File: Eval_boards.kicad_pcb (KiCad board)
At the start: 2 copper layers, 36 parts, among them J1 TC2030, J2 Conn_01x03_Pin, J3 Conn_02x07_Odd_Even, J4 Conn_01x07_Pin, J5 Conn_01x04_Pin, J6 Conn_02x07_Odd_Even, U1 STM32U031K8Ux, Y1 G83270025

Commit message: Early pcb project
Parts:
- removed J5: Conn_01x04_Pin, Connector_PinHeader_2.54mm:PinHeader_1x04_P2.54mm_Vertical
- removed J6: Conn_02x07_Odd_Even, Connector_PinHeader_2.54mm:PinHeader_2x07_P2.54mm_Vertical
- added C10: 40u, Capacitor_SMD:C_0603_1608Metric, B.Cu at (115.0, 85.3)
- added C11: 47n, Capacitor_SMD:C_0603_1608Metric, B.Cu at (116.6, 88.8)
- added C12: 40u, Capacitor_SMD:C_0603_1608Metric, B.Cu at (118.0, 92.7)
- added C13: 10u, Capacitor_SMD:C_0603_1608Metric, B.Cu at (132.2, 90.5)
- added C14: 4u7, Capacitor_SMD:C_0603_1608Metric, B.Cu at (113.5, 85.3)
- added C15: 10u, Capacitor_SMD:C_0603_1608Metric, B.Cu at (114.0, 95.0)
- added C16: 22u, Capacitor_SMD:C_0603_1608Metric, B.Cu at (107.6, 92.0)
- added C8: 1u, Capacitor_SMD:C_0603_1608Metric, B.Cu at (119.5, 82.0)
- added C9: 100n, Capacitor_SMD:C_0603_1608Metric, B.Cu at (118.0, 80.5)
- added D10: blue led, Diode_SMD:D_0603_1608Metric, F.Cu at (115.0, 75.0)
- added D100: blue led, Diode_SMD:D_0603_1608Metric, F.Cu at (95.0, 110.0)
- added D101: blue led, Diode_SMD:D_0603_1608Metric, F.Cu at (100.0, 110.0)
- added D102: blue led, Diode_SMD:D_0603_1608Metric, F.Cu at (105.0, 110.0)
- added D103: blue led, Diode_SMD:D_0603_1608Metric, F.Cu at (110.0, 110.0)
- added D104: blue led, Diode_SMD:D_0603_1608Metric, F.Cu at (115.0, 110.0)
- added D105: blue led, Diode_SMD:D_0603_1608Metric, F.Cu at (120.0, 110.0)
- added D106: blue led, Diode_SMD:D_0603_1608Metric, F.Cu at (125.0, 110.0)
- added D107: blue led, Diode_SMD:D_0603_1608Metric, F.Cu at (130.0, 110.0)
- added D108: blue led, Diode_SMD:D_0603_1608Metric, F.Cu at (135.0, 110.0)
- added D109: blue led, Diode_SMD:D_0603_1608Metric, F.Cu at (140.0, 110.0)
- added D11: blue led, Diode_SMD:D_0603_1608Metric, F.Cu at (120.0, 75.0)
- added D110: blue led, Diode_SMD:D_0603_1608Metric, F.Cu at (145.0, 110.0)
- added D111: blue led, Diode_SMD:D_0603_1608Metric, F.Cu at (150.0, 110.0)
- added D112: blue led, Diode_SMD:D_0603_1608Metric, F.Cu at (155.0, 110.0)
- added D113: blue led, Diode_SMD:D_0603_1608Metric, F.Cu at (85.0, 115.0)
- added D114: blue led, Diode_SMD:D_0603_1608Metric, F.Cu at (90.0, 115.0)
- added D115: blue led, Diode_SMD:D_0603_1608Metric, F.Cu at (95.0, 115.0)
- added D116: blue led, Diode_SMD:D_0603_1608Metric, F.Cu at (100.0, 115.0)
- added D117: blue led, Diode_SMD:D_0603_1608Metric, F.Cu at (105.0, 115.0)
- added D118: blue led, Diode_SMD:D_0603_1608Metric, F.Cu at (110.0, 115.0)
- added D119: blue led, Diode_SMD:D_0603_1608Metric, F.Cu at (115.0, 115.0)
- added D12: blue led, Diode_SMD:D_0603_1608Metric, F.Cu at (125.0, 75.0)
- added D120: blue led, Diode_SMD:D_0603_1608Metric, F.Cu at (120.0, 115.0)
- added D121: blue led, Diode_SMD:D_0603_1608Metric, F.Cu at (125.0, 115.0)
- added D122: blue led, Diode_SMD:D_0603_1608Metric, F.Cu at (130.0, 115.0)
- added D123: blue led, Diode_SMD:D_0603_1608Metric, F.Cu at (135.0, 115.0)
- added D124: blue led, Diode_SMD:D_0603_1608Metric, F.Cu at (140.0, 115.0)
- added D125: blue led, Diode_SMD:D_0603_1608Metric, F.Cu at (145.0, 115.0)
- added D126: blue led, Diode_SMD:D_0603_1608Metric, F.Cu at (150.0, 115.0)
- added D127: blue led, Diode_SMD:D_0603_1608Metric, F.Cu at (155.0, 115.0)
- added D128: blue led, Diode_SMD:D_0603_1608Metric, F.Cu at (90.0, 120.0)
- added D129: blue led, Diode_SMD:D_0603_1608Metric, F.Cu at (95.0, 120.0)
- added D13: blue led, Diode_SMD:D_0603_1608Metric, F.Cu at (130.0, 75.0)
- added D130: blue led, Diode_SMD:D_0603_1608Metric, F.Cu at (100.0, 120.0)
- added D131: blue led, Diode_SMD:D_0603_1608Metric, F.Cu at (105.0, 120.0)
- added D132: blue led, Diode_SMD:D_0603_1608Metric, F.Cu at (110.0, 120.0)
- added D133: blue led, Diode_SMD:D_0603_1608Metric, F.Cu at (115.0, 120.0)
- added D134: blue led, Diode_SMD:D_0603_1608Metric, F.Cu at (120.0, 120.0)
- added D135: blue led, Diode_SMD:D_0603_1608Metric, F.Cu at (125.0, 120.0)
- added D136: blue led, Diode_SMD:D_0603_1608Metric, F.Cu at (130.0, 120.0)
- added D137: blue led, Diode_SMD:D_0603_1608Metric, F.Cu at (135.0, 120.0)
- added D138: blue led, Diode_SMD:D_0603_1608Metric, F.Cu at (140.0, 120.0)
- added D139: blue led, Diode_SMD:D_0603_1608Metric, F.Cu at (145.0, 120.0)
- added D14: blue led, Diode_SMD:D_0603_1608Metric, F.Cu at (135.0, 75.0)
- added D140: blue led, Diode_SMD:D_0603_1608Metric, F.Cu at (150.0, 120.0)
- added D141: blue led, Diode_SMD:D_0603_1608Metric, F.Cu at (89.8, 125.0)
- added D142: blue led, Diode_SMD:D_0603_1608Metric, F.Cu at (95.0, 125.0)
- added D143: blue led, Diode_SMD:D_0603_1608Metric, F.Cu at (100.0, 125.0)
- added D144: blue led, Diode_SMD:D_0603_1608Metric, F.Cu at (105.0, 125.0)
- added D145: blue led, Diode_SMD:D_0603_1608Metric, F.Cu at (110.0, 125.0)
- added D146: blue led, Diode_SMD:D_0603_1608Metric, F.Cu at (115.0, 125.0)
- added D147: blue led, Diode_SMD:D_0603_1608Metric, F.Cu at (120.0, 125.0)
- added D148: blue led, Diode_SMD:D_0603_1608Metric, F.Cu at (125.0, 125.0)
- added D149: blue led, Diode_SMD:D_0603_1608Metric, F.Cu at (130.0, 125.0)
- added D15: blue led, Diode_SMD:D_0603_1608Metric, F.Cu at (140.0, 75.0)
- added D150: blue led, Diode_SMD:D_0603_1608Metric, F.Cu at (135.0, 125.0)
- added D151: blue led, Diode_SMD:D_0603_1608Metric, F.Cu at (140.0, 125.0)
- added D152: blue led, Diode_SMD:D_0603_1608Metric, F.Cu at (145.0, 125.0)
- added D153: blue led, Diode_SMD:D_0603_1608Metric, F.Cu at (150.0, 125.0)
- added D154: blue led, Diode_SMD:D_0603_1608Metric, F.Cu at (95.0, 130.0)
- added D155: blue led, Diode_SMD:D_0603_1608Metric, F.Cu at (100.0, 130.0)
- added D156: blue led, Diode_SMD:D_0603_1608Metric, F.Cu at (105.0, 130.0)
- added D157: blue led, Diode_SMD:D_0603_1608Metric, F.Cu at (110.0, 130.0)
- added D158: blue led, Diode_SMD:D_0603_1608Metric, F.Cu at (115.0, 130.0)
- added D159: blue led, Diode_SMD:D_0603_1608Metric, F.Cu at (120.0, 130.0)
- added D16: blue led, Diode_SMD:D_0603_1608Metric, F.Cu at (95.0, 80.0)
- added D160: blue led, Diode_SMD:D_0603_1608Metric, F.Cu at (125.0, 130.0)
- added D161: blue led, Diode_SMD:D_0603_1608Metric, F.Cu at (130.0, 130.0)
- added D162: blue led, Diode_SMD:D_0603_1608Metric, F.Cu at (135.0, 130.0)
- added D163: blue led, Diode_SMD:D_0603_1608Metric, F.Cu at (140.0, 130.0)
- added D164: blue led, Diode_SMD:D_0603_1608Metric, F.Cu at (145.0, 130.0)
- added D165: blue led, Diode_SMD:D_0603_1608Metric, F.Cu at (100.0, 135.0)
- added D166: blue led, Diode_SMD:D_0603_1608Metric, F.Cu at (105.0, 135.0)
- added D167: blue led, Diode_SMD:D_0603_1608Metric, F.Cu at (110.0, 135.0)
- added D168: blue led, Diode_SMD:D_0603_1608Metric, F.Cu at (115.0, 135.0)
- added D169: blue led, Diode_SMD:D_0603_1608Metric, F.Cu at (120.0, 135.0)
- added D17: blue led, Diode_SMD:D_0603_1608Metric, F.Cu at (100.0, 80.0)
- added D170: blue led, Diode_SMD:D_0603_1608Metric, F.Cu at (125.0, 135.0)
- added D171: blue led, Diode_SMD:D_0603_1608Metric, F.Cu at (130.0, 135.0)
- added D172: blue led, Diode_SMD:D_0603_1608Metric, F.Cu at (135.0, 135.0)
- added D173: blue led, Diode_SMD:D_0603_1608Metric, F.Cu at (140.0, 135.0)
- added D174: blue led, Diode_SMD:D_0603_1608Metric, F.Cu at (110.0, 140.0)
- added D175: blue led, Diode_SMD:D_0603_1608Metric, F.Cu at (115.0, 140.0)
- added D176: blue led, Diode_SMD:D_0603_1608Metric, F.Cu at (120.0, 140.0)
- added D177: blue led, Diode_SMD:D_0603_1608Metric, F.Cu at (125.0, 140.0)
- added D178: blue led, Diode_SMD:D_0603_1608Metric, F.Cu at (130.0, 140.0)
- added D179: blue led, Diode_SMD:D_0603_1608Metric, B.Cu at (125.7, 82.0)
- added D18: blue led, Diode_SMD:D_0603_1608Metric, F.Cu at (105.0, 80.0)
- added D19: blue led, Diode_SMD:D_0603_1608Metric, F.Cu at (110.0, 80.0)
- added D20: blue led, Diode_SMD:D_0603_1608Metric, F.Cu at (115.0, 80.0)
- added D21: blue led, Diode_SMD:D_0603_1608Metric, F.Cu at (120.0, 80.0)
- added D22: blue led, Diode_SMD:D_0603_1608Metric, F.Cu at (125.0, 80.0)
- added D23: blue led, Diode_SMD:D_0603_1608Metric, F.Cu at (130.0, 80.0)
- added D24: blue led, Diode_SMD:D_0603_1608Metric, F.Cu at (135.0, 80.0)
- added D25: blue led, Diode_SMD:D_0603_1608Metric, F.Cu at (140.0, 80.0)
- added D26: blue led, Diode_SMD:D_0603_1608Metric, F.Cu at (145.0, 80.0)
- added D27: blue led, Diode_SMD:D_0603_1608Metric, F.Cu at (90.0, 85.0)
- added D28: blue led, Diode_SMD:D_0603_1608Metric, F.Cu at (95.0, 85.0)
- added D29: blue led, Diode_SMD:D_0603_1608Metric, F.Cu at (100.0, 85.0)
- added D3: blue led, Diode_SMD:D_0603_1608Metric, F.Cu at (115.0, 70.0)
- added D30: blue led, Diode_SMD:D_0603_1608Metric, F.Cu at (105.0, 85.0)
- added D31: blue led, Diode_SMD:D_0603_1608Metric, F.Cu at (110.0, 85.0)
- added D32: blue led, Diode_SMD:D_0603_1608Metric, F.Cu at (115.0, 85.0)
- added D33: blue led, Diode_SMD:D_0603_1608Metric, F.Cu at (120.0, 85.0)
- added D34: blue led, Diode_SMD:D_0603_1608Metric, F.Cu at (125.0, 85.0)
- added D35: blue led, Diode_SMD:D_0603_1608Metric, F.Cu at (130.0, 85.0)
- added D36: blue led, Diode_SMD:D_0603_1608Metric, F.Cu at (135.0, 85.0)
- added D37: blue led, Diode_SMD:D_0603_1608Metric, F.Cu at (140.0, 85.0)
- added D38: blue led, Diode_SMD:D_0603_1608Metric, F.Cu at (145.0, 85.0)
- added D39: blue led, Diode_SMD:D_0603_1608Metric, F.Cu at (150.0, 85.0)
- added D4: blue led, Diode_SMD:D_0603_1608Metric, F.Cu at (120.0, 70.0)
- added D40: blue led, Diode_SMD:D_0603_1608Metric, F.Cu at (90.0, 90.0)
- added D41: blue led, Diode_SMD:D_0603_1608Metric, F.Cu at (95.0, 90.0)
- added D42: blue led, Diode_SMD:D_0603_1608Metric, F.Cu at (100.0, 90.0)
- added D43: blue led, Diode_SMD:D_0603_1608Metric, F.Cu at (105.0, 90.0)
- added D44: blue led, Diode_SMD:D_0603_1608Metric, F.Cu at (110.0, 90.0)
- added D45: blue led, Diode_SMD:D_0603_1608Metric, F.Cu at (115.0, 90.0)
- added D46: blue led, Diode_SMD:D_0603_1608Metric, F.Cu at (120.0, 90.0)
- added D47: blue led, Diode_SMD:D_0603_1608Metric, F.Cu at (125.0, 90.0)
- added D48: blue led, Diode_SMD:D_0603_1608Metric, F.Cu at (130.0, 90.0)
- added D49: blue led, Diode_SMD:D_0603_1608Metric, F.Cu at (135.0, 90.0)
- added D5: blue led, Diode_SMD:D_0603_1608Metric, F.Cu at (125.0, 70.0)
- added D50: blue led, Diode_SMD:D_0603_1608Metric, F.Cu at (140.0, 90.0)
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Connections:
- net ADC_BATTERY_MEASURE renamed POWER_MANAGEMENT_INTERRUPT
- C5 pad 1: Net-(U1-PC14) -> NRST
- C6 pad 1: GND -> Net-(U1-PC14)
- C6 pad 2: Net-(U1-PC15) -> GND
- C7 pad 1: NRST -> GND
- C7 pad 2: GND -> Net-(U1-PC15)
- D2 pad 1: unconnected-(D2-K-Pad1) -> G2R
- D2 pad 2: unconnected-(D2-A-Pad2) -> G1R
- J3 pad 1: G1 -> Net-(J3-Pin_1)
- J3 pad 2: G2 -> Net-(J3-Pin_2)
- J3 pad 3: G3 -> Net-(J3-Pin_3)
- J3 pad 4: G4 -> Net-(J3-Pin_4)
- J3 pad 5: G5 -> Net-(J3-Pin_5)
- J3 pad 6: G6 -> Net-(J3-Pin_6)
- J3 pad 7: G7 -> Net-(J3-Pin_7)
- J3 pad 8: G8 -> unconnected-(J3-Pin_8-Pad8)
- R1 pad 1: +3V3 -> NRST
- R1 pad 2: I2C_SDA -> +3V3
- R10 pad 1: G5 -> Net-(J3-Pin_6)
- R10 pad 2: unconnected-(R10-Pad2) -> +3V3
- R11 pad 1: G6 -> Net-(J3-Pin_7)
- R11 pad 2: unconnected-(R11-Pad2) -> PWR_WKUP
- R12 pad 1: G7 -> +3V3
- R12 pad 2: unconnected-(R12-Pad2) -> I2C_SDA
- R13 pad 1: G8 -> +3V3
- R13 pad 2: unconnected-(R13-Pad2) -> I2C_SCL
- R14 pad 1: G9 -> G1
- R14 pad 2: unconnected-(R14-Pad2) -> G1R
- R15 pad 1: G10 -> G2
- R15 pad 2: unconnected-(R15-Pad2) -> G2R
- R16 pad 1: G11 -> G3
- R16 pad 2: unconnected-(R16-Pad2) -> G3R
- R17 pad 1: G12 -> G4
- R17 pad 2: unconnected-(R17-Pad2) -> G4R
- R18 pad 1: G13 -> G5
- R18 pad 2: unconnected-(R18-Pad2) -> G5R
- R19 pad 1: G14 -> G6
- R19 pad 2: unconnected-(R19-Pad2) -> G6R
- R2 pad 1: +3V3 -> DIODE_TIM_CH
- R2 pad 2: I2C_SCL -> Net-(D1-A)
- R3 pad 1: +3V3 -> Net-(J3-Pin_1)
- R3 pad 2: I2C_SDA -> +3V3
- R4 pad 2: I2C_SCL -> I2C_SDA
- R5 pad 1: DIODE_TIM_CH -> +3V3
- R5 pad 2: Net-(D1-A) -> I2C_SCL
- R6 pad 1: G1 -> Net-(J3-Pin_2)
- R6 pad 2: unconnected-(R6-Pad2) -> GND
- R7 pad 1: G2 -> Net-(J3-Pin_3)
- R7 pad 2: unconnected-(R7-Pad2) -> I2C_SCL
- R8 pad 1: G3 -> Net-(J3-Pin_4)
- R8 pad 2: unconnected-(R8-Pad2) -> I2C_SDA
- R9 pad 1: G4 -> Net-(J3-Pin_5)
- R9 pad 2: unconnected-(R9-Pad2) -> GND
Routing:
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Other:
- copper layers 2 -> 4
- rule pad_to_mask_clearance: 0 -> 0.05

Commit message: Finished pcb project
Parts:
- removed J4: USB_C_Receptacle_PowerOnly_6P, Connector_USB:USB_C_Receptacle_GCT_USB4135-GF-A_6P_TopMnt_Horizontal
- removed R37, R38: 10k, Resistor_SMD:R_0603_1608Metric
- removed R39, R40, R42, R43, R44, R5, R6: 0R, Resistor_SMD:R_0603_1608Metric
- removed R41: 36k5, Resistor_SMD:R_0603_1608Metric
- removed TH1: 103AT-2, OptoDevice:R_LDR_4.9x4.2mm_P2.54mm_Vertical
- added C17: 100n, Capacitor_SMD:C_0603_1608Metric, B.Cu at (97.0, 112.7)
- added C18: 100n, Capacitor_SMD:C_0603_1608Metric, B.Cu at (103.5, 112.6)
- added JP1: SolderJumper_2_Open, Jumper:SolderJumper-2_P1.3mm_Open_TrianglePad1.0x1.5mm, B.Cu at (98.9, 99.8)
- added JP10: SolderJumper_2_Open, Jumper:SolderJumper-2_P1.3mm_Open_TrianglePad1.0x1.5mm, B.Cu at (132.8, 112.6)
- added JP2: SolderJumper_2_Open, Jumper:SolderJumper-2_P1.3mm_Open_TrianglePad1.0x1.5mm, B.Cu at (101.5, 99.8)
- added JP3: SolderJumper_2_Open, Jumper:SolderJumper-2_P1.3mm_Open_TrianglePad1.0x1.5mm, B.Cu at (101.7, 107.5)
- added JP4: SolderJumper_2_Open, Jumper:SolderJumper-2_P1.3mm_Open_TrianglePad1.0x1.5mm, B.Cu at (99.0, 107.5)
- added JP5: SolderJumper_2_Open, Jumper:SolderJumper-2_P1.3mm_Open_TrianglePad1.0x1.5mm, B.Cu at (87.8, 112.7)
- added JP6: SolderJumper_2_Open, Jumper:SolderJumper-2_P1.3mm_Open_TrianglePad1.0x1.5mm, B.Cu at (90.5, 112.7)
- added JP7: SolderJumper_2_Open, Jumper:SolderJumper-2_P1.3mm_Open_TrianglePad1.0x1.5mm, B.Cu at (132.8, 122.6)
- added JP8: SolderJumper_2_Open, Jumper:SolderJumper-2_P1.3mm_Open_TrianglePad1.0x1.5mm, B.Cu at (132.8, 117.4)
- added JP9: SolderJumper_2_Open, Jumper:SolderJumper-2_P1.3mm_Open_TrianglePad1.0x1.5mm, B.Cu at (124.6, 107.8)
- added U4: BMA400, BMA400:XDCR_BMA400, B.Cu at (100.0, 112.5)
- C1, C4, C5, D1, J1, R14, R15, R16, R17, R18, R19, R20, R3, R36, R4, U1, Y1: moved to B.Cu
- C10: value 40u -> 1u
- C11: value 47n -> 100n
- C13: value 10u -> 47n
- C15: value 10u -> 40u
- C16: value 22u -> 10u
- C2, C3: value 100n -> 8p; moved to B.Cu
- C6, C7: value 8p -> 100n; moved to B.Cu
- C8: value 1u -> 10u
- C9: value 100n -> 22u
- J2: footprint Connector_PinSocket_2.54mm:PinSocket_1x03_P2.54mm_Vertical -> Connector_JST:JST_GH_BM03B-GHS-TBT_1x03-1MP_P1.25mm_Vertical; moved to B.Cu
- J3: value Conn_01x08_Pin -> USB_C_Receptacle_PowerOnly_6P; footprint Connector_PinHeader_2.54mm:PinHeader_1x08_P2.54mm_Vertical -> Connector_USB:USB_C_Receptacle_GCT_USB4135-GF-A_6P_TopMnt_Horizontal; moved to B.Cu
- R1: value 10k -> 100R; moved to B.Cu
- R10, R11, R12, R13, R7, R8, R9: value 0R -> 100R; moved to B.Cu
- R2: value 100R -> 10k; moved to B.Cu
- R21, R22: value 100R -> 5k1; moved to B.Cu
- R23: value 100R -> 36k5; moved to B.Cu
- R24, R25: value 100R -> 0R; moved to B.Cu
- R26: value 100R -> 260R; moved to B.Cu
- R27: value 100R -> 2k2; moved to B.Cu
- R28: value 2k2 -> 10k
- R29: value 10k -> 5k23
- R30: value 5k1 -> 30k1
- R31: value 5k1 -> 10k
- R32: value 5k23 -> 10k
- R33: value 260R -> 10k
- R34: value 30k1 -> 10k
- R35: value 0R -> 10k; moved to B.Cu
- TP1: value USB 5V -> GND
- TP2: value BQ SYS -> USB 5V
- TP3: value BAT+ -> GND; footprint TestPoint:TestPoint_Pad_D2.5mm -> TestPoint:TestPoint_Pad_D2.0mm
- TP4: value GND -> 3V3
- TP5: value BAT- -> BQ SYS; footprint TestPoint:TestPoint_Pad_D2.5mm -> TestPoint:TestPoint_Pad_D2.0mm
- TP6: value 3V3 -> BAT+; footprint TestPoint:TestPoint_Pad_D2.0mm -> TestPoint:TestPoint_Pad_D2.5mm; moved to B.Cu
- TP7: value GND -> BAT-; footprint TestPoint:TestPoint_Pad_D2.0mm -> TestPoint:TestPoint_Pad_D2.5mm; moved to B.Cu
- U2: value BQ25895RTW -> TPS63900; footprint Package_DFN_QFN:Texas_RTW_WQFN-24-1EP_4x4mm_P0.5mm_EP2.7x2.7mm_ThermalVias -> Package_SON:WSON-10-1EP_2.5x2.5mm_P0.5mm_EP1.2x2mm_ThermalVias
- U3: value TPS63900 -> BQ25895RTW; footprint Package_SON:WSON-10-1EP_2.5x2.5mm_P0.5mm_EP1.2x2mm_ThermalVias -> Package_DFN_QFN:Texas_RTW_WQFN-24-1EP_4x4mm_P0.5mm_EP2.7x2.7mm_ThermalVias
- moved TP6 196.6 mm to (152.5, 97.7), turned to 180 degrees
- moved TP7 185.0 mm to (152.5, 112.5), turned to 180 degrees
- moved R23 162.3 mm to (137.4, 102.5)
- moved R24 161.0 mm to (137.4, 104.3), turned to 180 degrees
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- renumbered D69 to D10, D22 to D100, D34 to D101, D47 to D102, D61 to D103, D76 to D104, D91 to D105, D121 to D107, D135 to D108, D148 to D109, D84 to D11, D160 to D110, D170 to D111, D177 to D112, D6 to D113, D13 to D114, D23 to D115, D35 to D116, D48 to D117, D62 to D118, D77 to D119, D99 to D12, D92 to D120, D107 to D121, D136 to D123, D149 to D124, D161 to D125, D171 to D126, D178 to D127, D14 to D128, D24 to D129, D114 to D13, D36 to D130, D49 to D131, D63 to D132, D78 to D133, D93 to D134, D108 to D135, D123 to D136, D150 to D138, D162 to D139, D128 to D14, D172 to D140, D15 to D141, D25 to D142, D37 to D143, D50 to D144, D64 to D145, D79 to D146, D94 to D147, D109 to D148, D124 to D149, D141 to D15, D138 to D150, D163 to D152, D173 to D153, D26 to D154, D38 to D155, D51 to D156, D65 to D157, D80 to D158, D95 to D159, D110 to D160, D125 to D161, D139 to D162, D152 to D163, D39 to D165, D52 to D166, D66 to D167, D81 to D168, D96 to D169, D28 to D17, D111 to D170, D126 to D171, D140 to D172, D153 to D173, D67 to D174, D82 to D175, D97 to D176, D112 to D177, D127 to D178, D41 to D18, D55 to D19, D53 to D2, D70 to D20, D85 to D21, D100 to D22, D115 to D23, D129 to D24, D142 to D25, D154 to D26, D7 to D27, D17 to D28, D68 to D3, D42 to D30, D56 to D31, D71 to D32, D86 to D33, D101 to D34, D116 to D35, D130 to D36, D143 to D37, D155 to D38, D165 to D39, D83 to D4, D8 to D40, D18 to D41, D30 to D42, D57 to D44, D72 to D45, D87 to D46, D102 to D47, D117 to D48, D131 to D49, D98 to D5, D144 to D50, D156 to D51, D166 to D52, D2 to D53, D9 to D54, D19 to D55, D31 to D56, D44 to D57, D73 to D59, D113 to D6, D88 to D60, D103 to D61, D118 to D62, D132 to D63, D145 to D64, D157 to D65, D167 to D66, D174 to D67, D3 to D68, D10 to D69, D27 to D7, D20 to D70, D32 to D71, D45 to D72, D59 to D73, D89 to D75, D104 to D76, D119 to D77, D133 to D78, D146 to D79, D40 to D8, D158 to D80, D168 to D81, D175 to D82, D4 to D83, D11 to D84, D21 to D85, D33 to D86, D46 to D87, D60 to D88, D75 to D89, D54 to D9, D105 to D91, D120 to D92, D134 to D93, D147 to D94, D159 to D95, D169 to D96, D176 to D97, D5 to D98, D12 to D99
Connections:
- net SWCLK renamed /MCU/SWCLK
- net SWDIO renamed /MCU/SWDIO
- net SWO renamed /MCU/SWO
- net UART_RX renamed /MCU/UART_RX
- net UART_TX renamed /MCU/UART_TX
- C10 pad 1: Net-(U2-PMID) -> +5V
- C11 pad 1: Net-(C11-Pad1) -> +5V
- C11 pad 2: Net-(U2-BTST) -> GND
- C12 pad 1: VCC -> Net-(U3-PMID)
- C13 pad 2: GND -> Net-(U3-BTST)
- C14 pad 1: Net-(U2-REGN) -> Net-(U3-REGN)
- C15 pad 1: VCC -> +4V
- C16 pad 1: +3V3_BQ -> Net-(C16-Pad1)
- C2 pad 1: +3V3 -> Net-(U1-PC14)
- C3 pad 1: +3V3 -> GND
- C3 pad 2: GND -> Net-(U1-PC15)
- C5 pad 1: NRST -> +3V3
- C6 pad 1: Net-(U1-PC14) -> /MCU/NRST
- C7 pad 1: GND -> +3V3
- C7 pad 2: Net-(U1-PC15) -> GND
- C8 pad 1: +5V_USB -> +4V
- C9 pad 1: +5V_USB -> +3V3_BQ
- D14 pad 2: unconnected-(D128-A-Pad2) -> G10R
- D161 pad 2: unconnected-(D125-A-Pad2) -> G10R
- D171 pad 2: unconnected-(D126-A-Pad2) -> G10R
- D49 pad 2: unconnected-(D131-A-Pad2) -> G10R
- J1 pad 3: NRST -> /MCU/NRST
- L1 pad 1: Net-(C11-Pad1) -> Net-(U2-LX1)
- L1 pad 2: VCC -> Net-(U2-LX2)
- L2 pad 1: Net-(U3-LX1) -> Net-(C13-Pad1)
- L2 pad 2: Net-(U3-LX2) -> +4V
- R1 pad 1: NRST -> /MCU/DIODE_TIM_CH
- R1 pad 2: +3V3 -> Net-(D1-A)
- R10 pad 1: Net-(J3-Pin_6) -> /LED_DISPLAY/G4
- R10 pad 2: +3V3 -> G4R
- R11 pad 1: Net-(J3-Pin_7) -> /LED_DISPLAY/G5
- R11 pad 2: PWR_WKUP -> G5R
- R12 pad 1: +3V3 -> /LED_DISPLAY/G6
- R12 pad 2: I2C_SDA -> G6R
- R13 pad 1: +3V3 -> /LED_DISPLAY/G7
- R13 pad 2: I2C_SCL -> G7R
- R14 pad 1: G1 -> /LED_DISPLAY/G8
- R14 pad 2: G1R -> G8R
- R15 pad 1: G2 -> /LED_DISPLAY/G9
- R15 pad 2: G2R -> G9R
- R16 pad 1: G3 -> /LED_DISPLAY/G10
- R16 pad 2: G3R -> G10R
- R17 pad 1: G4 -> /LED_DISPLAY/G11
- R17 pad 2: G4R -> G11R
- R18 pad 1: G5 -> /LED_DISPLAY/G12
- R18 pad 2: G5R -> G12R
- R19 pad 1: G6 -> /LED_DISPLAY/G13
- R19 pad 2: G6R -> G13R
- R2 pad 1: DIODE_TIM_CH -> /MCU/NRST
- R2 pad 2: Net-(D1-A) -> +3V3
- R20 pad 1: G7 -> /LED_DISPLAY/G14
- R20 pad 2: G7R -> G14R
- R21 pad 1: G8 -> Net-(J3-CC2)
- R21 pad 2: G8R -> GND
- R22 pad 1: G9 -> Net-(J3-CC1)
- R22 pad 2: G9R -> GND
- R23 pad 1: G10 -> Net-(U2-CFG1)
- R23 pad 2: G10R -> GND
- R24 pad 1: G11 -> GND
- R24 pad 2: G11R -> Net-(U2-CFG2)
- R25 pad 1: G12 -> GND
- R25 pad 2: G12R -> Net-(U2-CFG3)
- R26 pad 1: G13 -> GND
- R26 pad 2: G13R -> Net-(U3-ILIM)
- R27 pad 1: G14 -> Net-(U3-STAT)
- R27 pad 2: G14R -> Net-(D179-K)
- R28 pad 1: Net-(U2-STAT) -> /MCU/INT
- R28 pad 2: Net-(D179-K) -> +3V3
- R29 pad 1: Net-(U2-DSEL) -> Net-(U3-TS)
- R29 pad 2: +5V_USB -> Net-(U3-REGN)
- R3 pad 1: Net-(J3-Pin_1) -> +3V3
- R3 pad 2: +3V3 -> /MCU/SDA_BQ
- R30 pad 1: Net-(J4-CC1) -> GND
- R30 pad 2: GND -> Net-(U3-TS)
- R31 pad 1: Net-(J4-CC2) -> /MCU/SDA_BQ
- R31 pad 2: GND -> +3V3
- R32 pad 1: Net-(U2-TS) -> Net-(U3-DSEL)
- R32 pad 2: Net-(U2-REGN) -> +4V
- R33 pad 2: Net-(U2-ILIM) -> Net-(U3-TS)
- R34 pad 1: GND -> /MCU/SCL_BQ
- R34 pad 2: Net-(U2-TS) -> +3V3
- R35 pad 1: VCC -> /ACCELEROMETER/SCL_A
- R35 pad 2: +3V3_BQ -> +3V3
- R36 pad 1: /MCU/INT -> /ACCELEROMETER/SDA_A
- R36 pad 2: VCC -> +3V3
- R4 pad 2: I2C_SDA -> /MCU/SCL_BQ
- R7 pad 1: Net-(J3-Pin_3) -> /LED_DISPLAY/G1
- R7 pad 2: I2C_SCL -> G1R
- R8 pad 1: Net-(J3-Pin_4) -> /LED_DISPLAY/G2
- R8 pad 2: I2C_SDA -> G2R
- R9 pad 1: Net-(J3-Pin_5) -> /LED_DISPLAY/G3
- R9 pad 2: GND -> G3R
- TP1 pad 1: +5V_USB -> GND
- TP2 pad 1: VCC -> +5V
- TP3 pad 1: Net-(C13-Pad1) -> GND
- TP4 pad 1: GND -> +3V3_BQ
- TP5 pad 1: GND -> +4V
- TP6 pad 1: +3V3_BQ -> Net-(C16-Pad1)
- U1 pad 10: DIODE_TIM_CH -> /MCU/INT
- U1 pad 11: POWER_MANAGEMENT_INTERRUPT -> /MCU/DIODE_TIM_CH
- U1 pad 12: I2C_SDA -> /MCU/SDA_BQ
- U1 pad 13: I2C_SDL -> /MCU/SCL_BQ
- U1 pad 14: G14 -> /LED_DISPLAY/G14
- U1 pad 15: G13 -> /LED_DISPLAY/G13
- U1 pad 18: G12 -> /LED_DISPLAY/G12
- U1 pad 19: G11 -> /LED_DISPLAY/G11
- U1 pad 20: G10 -> /LED_DISPLAY/G10
- U1 pad 21: G9 -> /LED_DISPLAY/G9
- U1 pad 22: G8 -> /LED_DISPLAY/G8
- U1 pad 25: G7 -> /LED_DISPLAY/G7
- U1 pad 27: G6 -> /LED_DISPLAY/G6
- U1 pad 28: G5 -> /LED_DISPLAY/G5
- U1 pad 29: G4 -> /LED_DISPLAY/G4
- U1 pad 30: G3 -> /LED_DISPLAY/G3
- U1 pad 31: G2 -> /LED_DISPLAY/G2
- U1 pad 4: NRST -> /MCU/NRST
- U1 pad 6: G1 -> /LED_DISPLAY/G1
- U1 pad 7: PWR_WKUP -> /MCU/PWR_WKUP
- U2 pad 1: +5V_USB -> +4V
- U2 pad 10: Net-(U2-ILIM) -> +4V
- U2 pad 11: Net-(U2-TS) -> GND
- U2 pad 2: unconnected-(U2-D+-Pad2) -> +4V
- U2 pad 3: unconnected-(U2-D--Pad3) -> Net-(U2-CFG1)
- U2 pad 4: Net-(U2-STAT) -> Net-(U2-CFG2)
- U2 pad 5: BQ_SCL -> Net-(U2-CFG3)
- U2 pad 6: BQ_SDA -> +3V3_BQ
- U2 pad 7: BQ_INT -> Net-(U2-LX2)
- U2 pad 9: GND -> Net-(U2-LX1)
- U3 pad 1: VCC -> +5V
- U3 pad 10: VCC -> Net-(U3-ILIM)
- U3 pad 11: GND -> Net-(U3-TS)
- U3 pad 2: VCC -> unconnected-(U3-D+-Pad2)
- U3 pad 3: Net-(U3-CFG1) -> unconnected-(U3-D--Pad3)
- U3 pad 4: Net-(U3-CFG2) -> Net-(U3-STAT)
- U3 pad 5: Net-(U3-CFG3) -> /POWER_MANAGEMENT/BQ_SCL
- U3 pad 6: +3V3_BQ -> /POWER_MANAGEMENT/BQ_SDA
- U3 pad 7: Net-(U3-LX2) -> /POWER_MANAGEMENT/BQ_INT
- U3 pad 9: Net-(U3-LX1) -> GND
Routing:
- net G2R: track 0.00 -> 301.0 mm, vias 0 -> 16
- net G8R: track 0.00 -> 280.6 mm, vias 0 -> 18
- net G4R: track 0.00 -> 269.7 mm, vias 0 -> 17
- net G14R: track 0.00 -> 267.3 mm, vias 0 -> 16
- net G6R: track 0.00 -> 265.7 mm, vias 0 -> 18
- net G5R: track 0.00 -> 263.9 mm, vias 0 -> 22
- net G7R: track 0.00 -> 256.6 mm, vias 0 -> 15
- net G1R: track 0.00 -> 250.4 mm, vias 0 -> 16
- net G9R: track 0.00 -> 249.5 mm, vias 0 -> 17
- net G3R: track 0.00 -> 249.2 mm, vias 0 -> 13
- net G13R: track 0.00 -> 240.3 mm, vias 0 -> 15
- net G11R: track 0.00 -> 236.1 mm, vias 0 -> 17
- net G12R: track 0.00 -> 224.5 mm, vias 0 -> 15
- net G10R: track 0.00 -> 223.4 mm, vias 0 -> 17
- net +3V3: track 0.00 -> 197.1 mm, vias 0 -> 17
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- added copper zone on B.Cu, net GND
- added copper zone on F.Cu, net GND
- added copper zone on In1.Cu, net GND
- added copper zone on In2.Cu, net GND
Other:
- board outline added: 88 x 88 mm

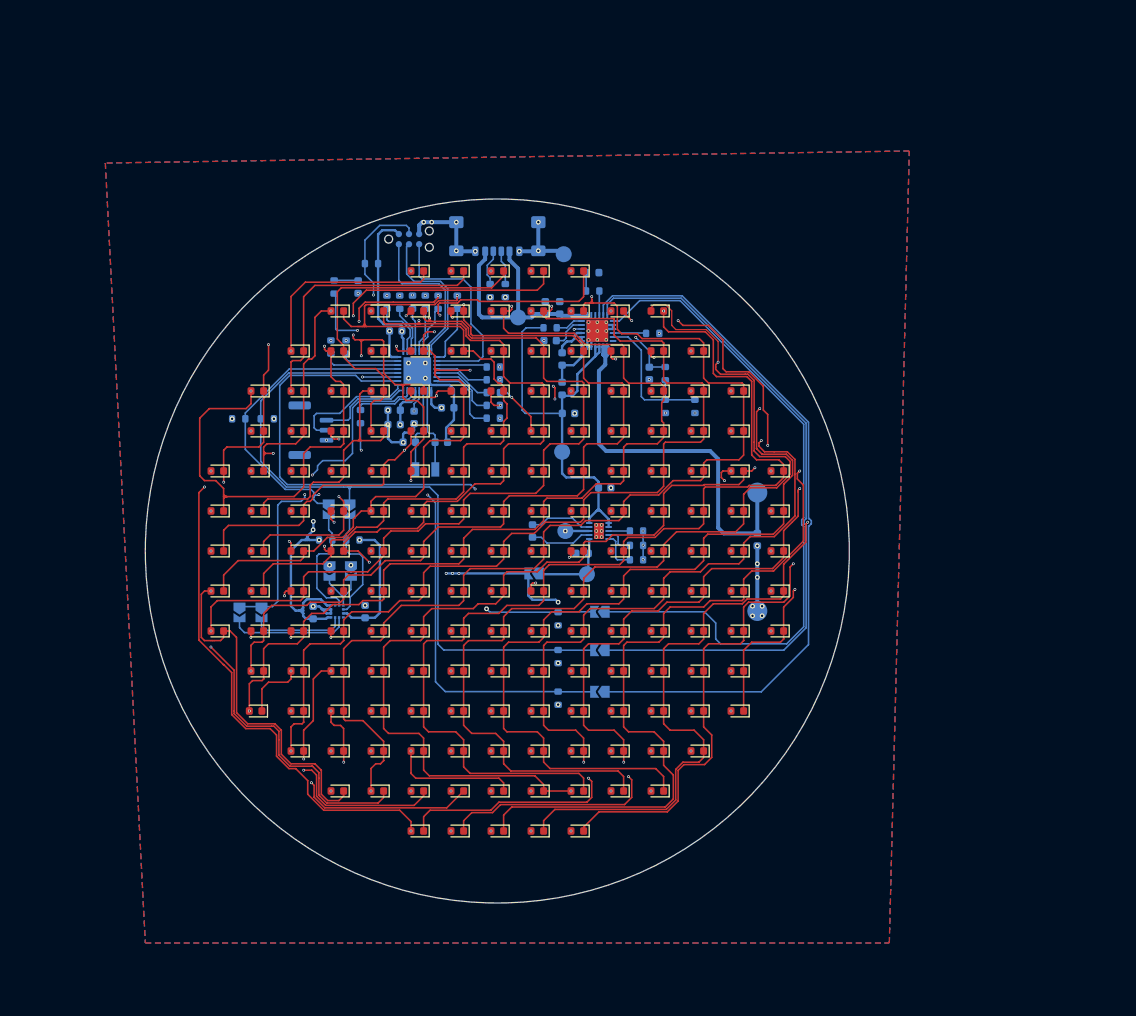
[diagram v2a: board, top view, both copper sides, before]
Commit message: Add new mcu and better leds layout
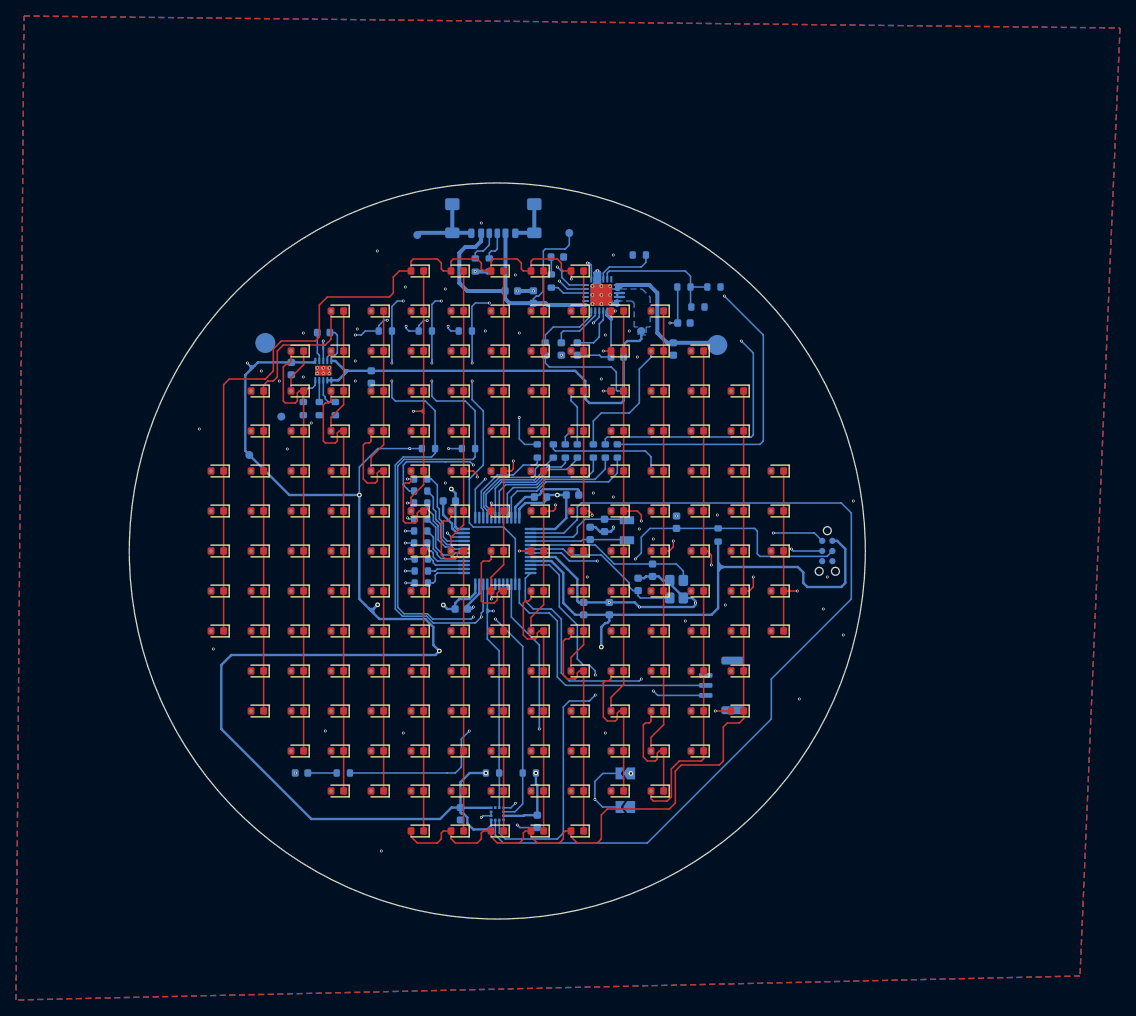
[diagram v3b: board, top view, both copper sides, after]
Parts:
- removed JP10, JP3, JP4, JP5, JP6, JP7, JP8, JP9: SolderJumper_2_Open, Jumper:SolderJumper-2_P1.3mm_Open_TrianglePad1.0x1.5mm
- removed TP1, TP3: GND, TestPoint:TestPoint_Pad_D2.0mm
- removed TP2: USB 5V, TestPoint:TestPoint_Pad_D2.0mm
- removed TP4: 3V3, TestPoint:TestPoint_Pad_D2.0mm
- removed TP5: BQ SYS, TestPoint:TestPoint_Pad_D2.0mm
- removed TP6: BAT+, TestPoint:TestPoint_Pad_D2.5mm
- removed TP7: BAT-, TestPoint:TestPoint_Pad_D2.5mm
- added 3V3: 3V3, TestPoint:TestPoint_Pad_D1.0mm, B.Cu at (89.0, 93.0)
- added 5V: USB 5V, TestPoint:TestPoint_Pad_D1.0mm, B.Cu at (129.0, 65.2)
- added BAT+: BAT+, TestPoint:TestPoint_Pad_D2.5mm, B.Cu at (147.5, 79.2)
- added BAT-: BAT-, TestPoint:TestPoint_Pad_D2.5mm, B.Cu at (91.0, 79.0)
- added C19: 10u, Capacitor_SMD:C_0603_1608Metric, B.Cu at (104.2, 83.2)
- added C20: 22u, Capacitor_SMD:C_0603_1608Metric, B.Cu at (94.2, 82.2)
- added C21: 100n, Capacitor_SMD:C_0603_1608Metric, B.Cu at (125.0, 138.8)
- added C22: 100n, Capacitor_SMD:C_0603_1608Metric, B.Cu at (115.4, 137.8)
- added GND: GND, TestPoint:TestPoint_Pad_D1.0mm, B.Cu at (93.0, 88.2)
- added GND: GND, TestPoint:TestPoint_Pad_D1.0mm, B.Cu at (110.0, 65.5)
- added R5: 100R, Resistor_SMD:R_0603_1608Metric, B.Cu at (135.0, 92.5)
- added R6: 100R, Resistor_SMD:R_0603_1608Metric, B.Cu at (133.5, 92.5)
- added V_SYS: BQ SYS, TestPoint:TestPoint_Pad_D1.0mm, B.Cu at (138.0, 77.5)
- added Y2: G83270025, Crystal:Crystal_SMD_3215-2Pin_3.2x1.5mm, B.Cu at (136.2, 102.4)
- C10: value 1u -> 8p
- C11: value 100n -> 8p
- C12: value 40u -> 1u
- C13: value 47n -> 100n
- C14: value 4u7 -> 40u
- C15: value 40u -> 47n
- C17: value 100n -> 10u
- C18: value 100n -> 4u7
- C2, C3: value 8p -> 100n
- C8: value 10u -> 3p
- C9: value 22u -> 3p
- R1: value 100R -> 10k
- R2: value 10k -> 100R
- R21: value 5k1 -> 2k2
- R22: value 5k1 -> 10k
- R23: value 36k5 -> 5k1
- R24: value 0R -> 5k1
- R25: value 0R -> 5k23
- R26: value 260R -> 270R
- R27: value 2k2 -> 30k1
- R29: value 5k23 -> 10k
- R30: value 30k1 -> 10k
- R32: value 10k -> 36k5
- R33, R34: value 10k -> 0R
- U1: value STM32U031K8Ux -> STM32L051C6Tx; footprint Package_DFN_QFN:QFN-32-1EP_5x5mm_P0.5mm_EP3.45x3.45mm -> Package_QFP:LQFP-48_7x7mm_P0.5mm
- U2: value TPS63900 -> BQ25895RTW; footprint Package_SON:WSON-10-1EP_2.5x2.5mm_P0.5mm_EP1.2x2mm_ThermalVias -> Package_DFN_QFN:Texas_RTW_WQFN-24-1EP_4x4mm_P0.5mm_EP2.7x2.7mm_ThermalVias
- U3: value BQ25895RTW -> TPS63900; footprint Package_DFN_QFN:Texas_RTW_WQFN-24-1EP_4x4mm_P0.5mm_EP2.7x2.7mm_ThermalVias -> Package_SON:WSON-10-1EP_2.5x2.5mm_P0.5mm_EP1.2x2mm_ThermalVias
- Y1: value G83270025 -> 25.00M-SMDHC49S; footprint Crystal:Crystal_SMD_3215-2Pin_3.2x1.5mm -> Crystal:Crystal_SMD_3225-4Pin_3.2x2.5mm
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- renumbered D69 to D10, D22 to D100, D34 to D101, D47 to D102, D61 to D103, D76 to D104, D91 to D105, D121 to D107, D135 to D108, D148 to D109, D84 to D11, D160 to D110, D170 to D111, D177 to D112, D6 to D113, D13 to D114, D23 to D115, D35 to D116, D48 to D117, D62 to D118, D77 to D119, D99 to D12, D92 to D120, D107 to D121, D136 to D123, D149 to D124, D161 to D125, D171 to D126, D178 to D127, D14 to D128, D24 to D129, D114 to D13, D36 to D130, D49 to D131, D63 to D132, D78 to D133, D93 to D134, D108 to D135, D123 to D136, D150 to D138, D162 to D139, D128 to D14, D172 to D140, D15 to D141, D25 to D142, D37 to D143, D50 to D144, D64 to D145, D79 to D146, D94 to D147, D109 to D148, D124 to D149, D141 to D15, D138 to D150, D163 to D152, D173 to D153, D26 to D154, D38 to D155, D51 to D156, D65 to D157, D80 to D158, D95 to D159, D110 to D160, D125 to D161, D139 to D162, D152 to D163, D39 to D165, D52 to D166, D66 to D167, D81 to D168, D96 to D169, D28 to D17, D111 to D170, D126 to D171, D140 to D172, D153 to D173, D67 to D174, D82 to D175, D97 to D176, D112 to D177, D127 to D178, D41 to D18, D55 to D19, D53 to D2, D70 to D20, D85 to D21, D100 to D22, D115 to D23, D129 to D24, D142 to D25, D154 to D26, D7 to D27, D17 to D28, D68 to D3, D42 to D30, D56 to D31, D71 to D32, D86 to D33, D101 to D34, D116 to D35, D130 to D36, D143 to D37, D155 to D38, D165 to D39, D83 to D4, D8 to D40, D18 to D41, D30 to D42, D57 to D44, D72 to D45, D87 to D46, D102 to D47, D117 to D48, D131 to D49, D98 to D5, D144 to D50, D156 to D51, D166 to D52, D2 to D53, D9 to D54, D19 to D55, D31 to D56, D44 to D57, D73 to D59, D113 to D6, D88 to D60, D103 to D61, D118 to D62, D132 to D63, D145 to D64, D157 to D65, D167 to D66, D174 to D67, D3 to D68, D10 to D69, D27 to D7, D20 to D70, D32 to D71, D45 to D72, D59 to D73, D89 to D75, D104 to D76, D119 to D77, D133 to D78, D146 to D79, D40 to D8, D158 to D80, D168 to D81, D175 to D82, D4 to D83, D11 to D84, D21 to D85, D33 to D86, D46 to D87, D60 to D88, D75 to D89, D54 to D9, D105 to D91, D120 to D92, D134 to D93, D147 to D94, D159 to D95, D169 to D96, D176 to D97, D5 to D98, D12 to D99
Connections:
- C10 pad 1: +5V -> /MCU/OSC32_IN
- C11 pad 1: +5V -> GND
- C11 pad 2: GND -> /MCU/OSC32_OUT
- C12 pad 1: Net-(U3-PMID) -> +5V
- C13 pad 1: Net-(C13-Pad1) -> +5V
- C13 pad 2: Net-(U3-BTST) -> GND
- C14 pad 1: Net-(U3-REGN) -> Net-(U2-PMID)
- C15 pad 1: +4V -> Net-(C15-Pad1)
- C15 pad 2: GND -> Net-(U2-BTST)
- C16 pad 1: Net-(C16-Pad1) -> +4V
- C17 pad 1: +3V3 -> Net-(C17-Pad1)
- C18 pad 1: +3V3 -> Net-(U2-REGN)
- C2 pad 1: Net-(U1-PC14) -> +3V3
- C3 pad 1: GND -> +3V3
- C3 pad 2: Net-(U1-PC15) -> GND
- C6 pad 1: /MCU/NRST -> +3V3
- C7 pad 1: +3V3 -> /MCU/NRST
- C8 pad 1: +4V -> /MCU/OSC_IN
- C9 pad 1: +3V3_BQ -> GND
- C9 pad 2: GND -> /MCU/OSC_OUT
- D10 pad 1: G10R -> G8R
- D10 pad 2: G1R -> G2R
- D100 pad 1: G9R -> G3R
- D100 pad 2: G8R -> G9R
- D101 pad 1: G10R -> G4R
- D101 pad 2: G8R -> G9R
- D102 pad 1: G11R -> G5R
- D102 pad 2: G8R -> G9R
- D103 pad 1: G12R -> G6R
- D103 pad 2: G8R -> G9R
- D104 pad 1: G13R -> G7R
- D104 pad 2: G8R -> G9R
- D105 pad 1: G14R -> G8R
- D105 pad 2: G8R -> G9R
- D106 pad 1: G1R -> G10R
- D107 pad 1: G2R -> G11R
- D108 pad 1: G3R -> G12R
- D109 pad 1: G4R -> G13R
- D11 pad 1: G11R -> G9R
- D11 pad 2: G1R -> G2R
- D110 pad 1: G5R -> G14R
- D111 pad 1: G6R -> G15R
- D112 pad 1: G7R -> G16R
- D113 pad 1: G8R -> G1R
- D113 pad 2: G9R -> G10R
- D114 pad 1: G10R -> G2R
- D114 pad 2: G9R -> G10R
- D115 pad 1: G11R -> G3R
- D115 pad 2: G9R -> G10R
- D116 pad 1: G12R -> G4R
- D116 pad 2: G9R -> G10R
- D117 pad 1: G13R -> G5R
- D117 pad 2: G9R -> G10R
- D118 pad 1: G14R -> G6R
- D118 pad 2: G9R -> G10R
- D119 pad 1: G1R -> G7R
- D12 pad 1: G12R -> G10R
- D12 pad 2: G1R -> G2R
- D120 pad 1: G2R -> G8R
- D121 pad 1: G3R -> G9R
- D122 pad 1: G4R -> G11R
- D123 pad 1: G5R -> G12R
- D124 pad 1: G6R -> G13R
- D125 pad 1: G7R -> G14R
- D126 pad 1: G8R -> G15R
- D127 pad 1: G9R -> G16R
- D128 pad 1: G11R -> G2R
- D128 pad 2: G10R -> G11R
- D129 pad 1: G12R -> G3R
- D129 pad 2: G10R -> G11R
- D13 pad 1: G13R -> G11R
- D13 pad 2: G1R -> G2R
- D130 pad 1: G13R -> G4R
- D130 pad 2: G10R -> G11R
- D131 pad 1: G14R -> G5R
- D131 pad 2: G10R -> G11R
- D132 pad 1: G1R -> G6R
- D133 pad 1: G2R -> G7R
- D134 pad 1: G3R -> G8R
- D135 pad 1: G4R -> G9R
- D136 pad 1: G5R -> G10R
- D137 pad 1: G6R -> G12R
- D138 pad 1: G7R -> G13R
- D139 pad 1: G8R -> G14R
- D14 pad 1: G14R -> G12R
- D14 pad 2: G1R -> G2R
- D140 pad 1: G9R -> G15R
- D141 pad 1: G10R -> G2R
- D141 pad 2: G11R -> G12R
- D142 pad 1: G12R -> G3R
- D142 pad 2: G11R -> G12R
- D143 pad 1: G13R -> G4R
- D143 pad 2: G11R -> G12R
- D144 pad 1: G14R -> G5R
- D144 pad 2: G11R -> G12R
- D145 pad 1: G1R -> G6R
- D146 pad 1: G2R -> G7R
- D147 pad 1: G3R -> G8R
- D148 pad 1: G4R -> G9R
- D149 pad 1: G5R -> G10R
- D15 pad 1: G1R -> G13R
- D150 pad 1: G6R -> G11R
- D151 pad 1: G7R -> G13R
- D152 pad 1: G8R -> G14R
- D153 pad 1: G9R -> G15R
- D154 pad 1: G10R -> G3R
- D154 pad 2: G12R -> G13R
- D155 pad 1: G11R -> G4R
- D155 pad 2: G12R -> G13R
- D156 pad 1: G13R -> G5R
- D156 pad 2: G12R -> G13R
- D157 pad 1: G14R -> G6R
- D157 pad 2: G12R -> G13R
- D158 pad 1: G1R -> G7R
- D159 pad 1: G2R -> G8R
- D16 pad 1: G3R -> G4R
- D16 pad 2: G2R -> G3R
- D160 pad 1: G3R -> G9R
- D161 pad 1: G4R -> G10R
- D162 pad 1: G5R -> G11R
- D163 pad 1: G6R -> G12R
- D164 pad 1: G7R -> G14R
- D165 pad 1: G8R -> G4R
- D165 pad 2: G13R -> G14R
- D166 pad 1: G9R -> G5R
- D166 pad 2: G13R -> G14R
- D167 pad 1: G10R -> G6R
- D167 pad 2: G13R -> G14R
- D168 pad 1: G11R -> G7R
- D168 pad 2: G13R -> G14R
- D169 pad 1: G12R -> G8R
- D169 pad 2: G13R -> G14R
- D17 pad 1: G4R -> G5R
- D17 pad 2: G2R -> G3R
- D170 pad 1: G14R -> G9R
- D170 pad 2: G13R -> G14R
- D171 pad 1: G1R -> G10R
- D172 pad 1: G2R -> G11R
- D173 pad 1: G3R -> G12R
- D174 pad 1: G4R -> G6R
- D174 pad 2: G14R -> G15R
- D175 pad 1: G5R -> G7R
- D175 pad 2: G14R -> G15R
- D176 pad 1: G6R -> G8R
- D176 pad 2: G14R -> G15R
- D177 pad 1: G7R -> G9R
- D177 pad 2: G14R -> G15R
- D178 pad 1: G8R -> G10R
- D178 pad 2: G14R -> G15R
- D18 pad 1: G5R -> G6R
- D18 pad 2: G2R -> G3R
- D19 pad 1: G6R -> G7R
- D19 pad 2: G2R -> G3R
- D2 pad 1: G2R -> G7R
- D20 pad 1: G7R -> G8R
- D20 pad 2: G2R -> G3R
- D21 pad 1: G8R -> G9R
- D21 pad 2: G2R -> G3R
- D22 pad 1: G9R -> G10R
- D22 pad 2: G2R -> G3R
- D23 pad 1: G10R -> G11R
- D23 pad 2: G2R -> G3R
- D24 pad 1: G11R -> G12R
- D24 pad 2: G2R -> G3R
- D25 pad 1: G12R -> G13R
- D25 pad 2: G2R -> G3R
- D26 pad 1: G13R -> G14R
- D26 pad 2: G2R -> G3R
- D27 pad 1: G14R -> G2R
- D27 pad 2: G2R -> G4R
- D28 pad 1: G1R -> G3R
- D28 pad 2: G3R -> G4R
- D29 pad 1: G2R -> G5R
- D29 pad 2: G3R -> G4R
- D3 pad 1: G3R -> G8R
- D30 pad 1: G4R -> G6R
- D30 pad 2: G3R -> G4R
- D31 pad 1: G5R -> G7R
- D31 pad 2: G3R -> G4R
- D32 pad 1: G6R -> G8R
- D32 pad 2: G3R -> G4R
- D33 pad 1: G7R -> G9R
- D33 pad 2: G3R -> G4R
- D34 pad 1: G8R -> G10R
- D34 pad 2: G3R -> G4R
- D35 pad 1: G9R -> G11R
- D35 pad 2: G3R -> G4R
- D36 pad 1: G10R -> G12R
- D36 pad 2: G3R -> G4R
- D37 pad 1: G11R -> G13R
- D37 pad 2: G3R -> G4R
- D38 pad 1: G12R -> G14R
- D38 pad 2: G3R -> G4R
- D39 pad 1: G13R -> G15R
- D39 pad 2: G3R -> G4R
- D4 pad 1: G4R -> G9R
- D40 pad 1: G14R -> G2R
- D40 pad 2: G3R -> G5R
- D41 pad 1: G1R -> G3R
- D41 pad 2: G4R -> G5R
- D42 pad 1: G2R -> G4R
- D42 pad 2: G4R -> G5R
- D43 pad 1: G3R -> G6R
- D43 pad 2: G4R -> G5R
- D44 pad 1: G5R -> G7R
- D44 pad 2: G4R -> G5R
- D45 pad 1: G6R -> G8R
- D45 pad 2: G4R -> G5R
- D46 pad 1: G7R -> G9R
- D46 pad 2: G4R -> G5R
- D47 pad 1: G8R -> G10R
- D47 pad 2: G4R -> G5R
- D48 pad 1: G9R -> G11R
- D48 pad 2: G4R -> G5R
- D49 pad 1: G10R -> G12R
- D49 pad 2: G4R -> G5R
- D5 pad 1: G5R -> G10R
- D50 pad 1: G11R -> G13R
- D50 pad 2: G4R -> G5R
- D51 pad 1: G12R -> G14R
- D51 pad 2: G4R -> G5R
- D52 pad 1: G13R -> G15R
- D52 pad 2: G4R -> G5R
- D53 pad 1: G14R -> G1R
- D53 pad 2: G4R -> G6R
- D54 pad 1: G1R -> G2R
- D54 pad 2: G5R -> G6R
- D55 pad 1: G2R -> G3R
- D55 pad 2: G5R -> G6R
- D56 pad 1: G3R -> G4R
- D56 pad 2: G5R -> G6R
- D57 pad 1: G4R -> G5R
- D57 pad 2: G5R -> G6R
- D58 pad 1: G6R -> G7R
- D58 pad 2: G5R -> G6R
- D59 pad 1: G7R -> G8R
- D59 pad 2: G5R -> G6R
- D6 pad 1: G6R -> G11R
- D60 pad 1: G8R -> G9R
- D60 pad 2: G5R -> G6R
- D61 pad 1: G9R -> G10R
- D61 pad 2: G5R -> G6R
- D62 pad 1: G10R -> G11R
- D62 pad 2: G5R -> G6R
- D63 pad 1: G11R -> G12R
- D63 pad 2: G5R -> G6R
- D64 pad 1: G12R -> G13R
- D64 pad 2: G5R -> G6R
- D65 pad 1: G13R -> G14R
- D65 pad 2: G5R -> G6R
- D66 pad 1: G14R -> G15R
- D66 pad 2: G5R -> G6R
- D67 pad 1: G1R -> G16R
- D68 pad 1: G2R -> G1R
- D68 pad 2: G6R -> G7R
- D69 pad 1: G3R -> G2R
- D69 pad 2: G6R -> G7R
- D7 pad 1: G7R -> G5R
- D7 pad 2: G1R -> G2R
- D70 pad 1: G4R -> G3R
- D70 pad 2: G6R -> G7R
- D71 pad 1: G5R -> G4R
- D71 pad 2: G6R -> G7R
- D72 pad 1: G7R -> G5R
- D72 pad 2: G6R -> G7R
- D73 pad 1: G8R -> G6R
- D73 pad 2: G6R -> G7R
- D74 pad 1: G9R -> G8R
- D74 pad 2: G6R -> G7R
- D75 pad 1: G10R -> G9R
- D75 pad 2: G6R -> G7R
- D76 pad 1: G11R -> G10R
- D76 pad 2: G6R -> G7R
- D77 pad 1: G12R -> G11R
- D77 pad 2: G6R -> G7R
- D78 pad 1: G13R -> G12R
- D78 pad 2: G6R -> G7R
- D79 pad 1: G14R -> G13R
- D79 pad 2: G6R -> G7R
- D8 pad 1: G8R -> G6R
- D8 pad 2: G1R -> G2R
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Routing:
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- added copper zone on B.Cu, net +4V
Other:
- board size 88 x 88 mm -> 92 x 92 mm
